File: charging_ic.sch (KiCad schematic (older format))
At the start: 6 parts, among them IC3 MCP73811T-420I_OT, Q1 Q_PMOS_DSG

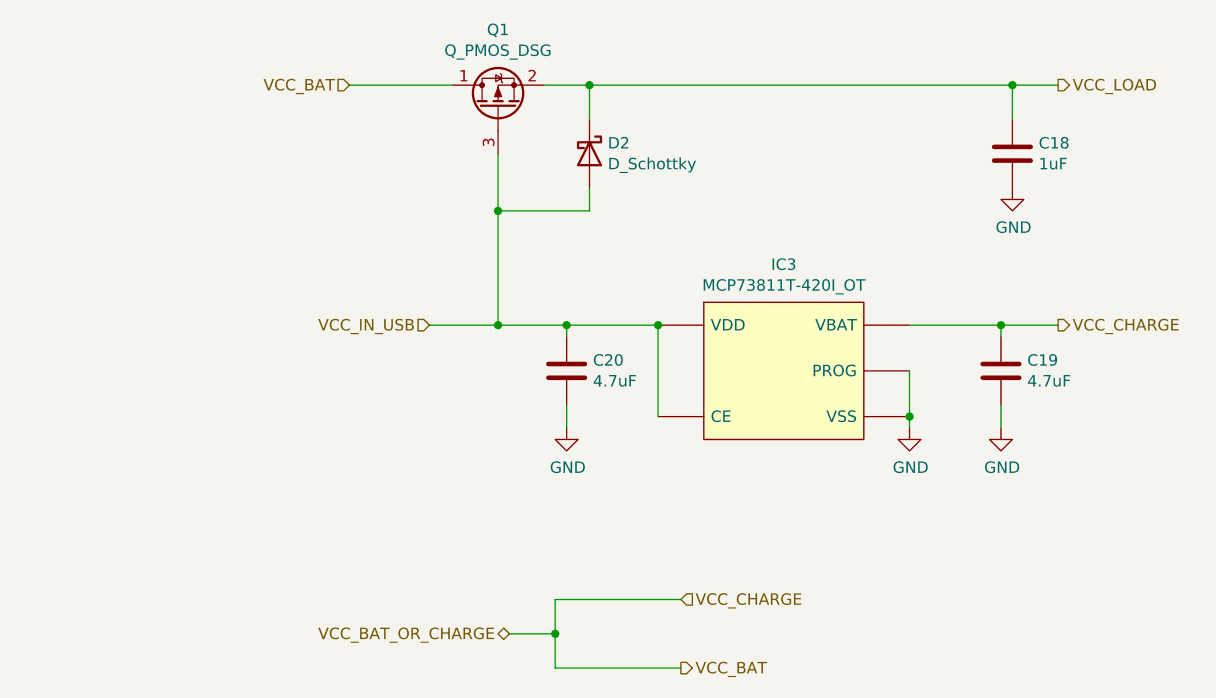
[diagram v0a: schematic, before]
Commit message: Fixed some symbols, assigned some footprints, and made wire labels
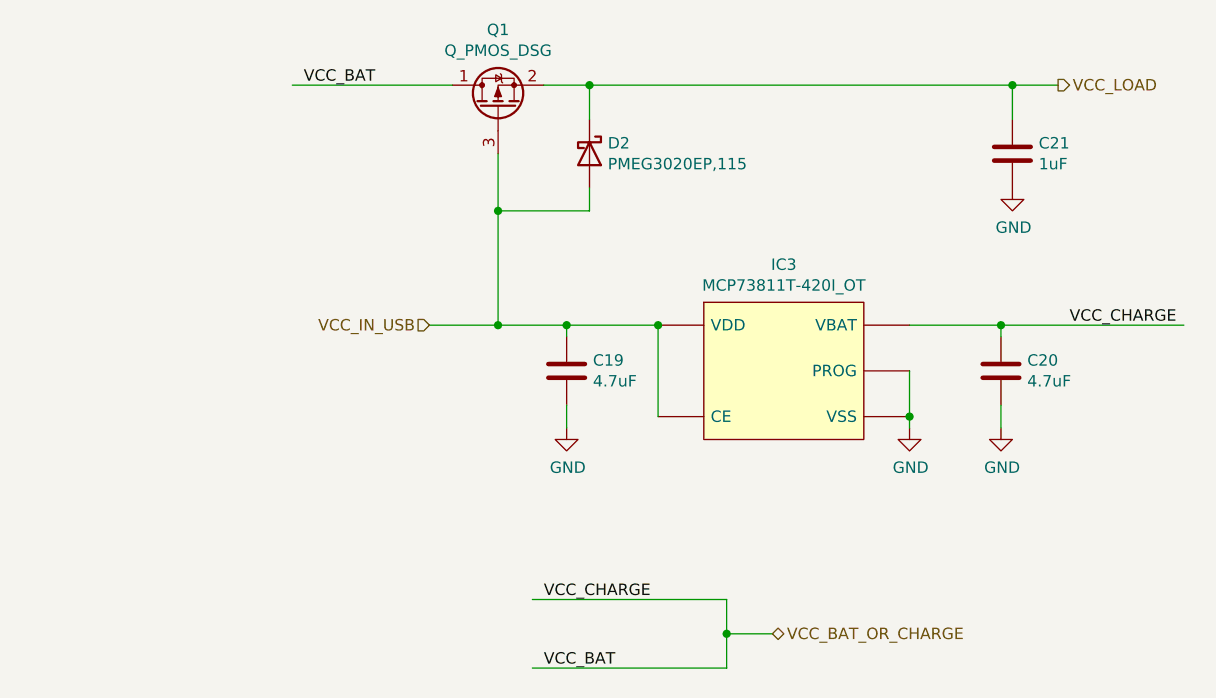
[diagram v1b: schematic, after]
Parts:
- removed D2: D_Schottky, symbol Device:D_Schottky
- added D2: PMEG3020EP,115, Diode_Skywire:SODFL4725X110N, symbol Diode_Shotkey:PMEG3020EP,115
- IC3: footprint SOT95P270X145-5N -> Charging_IC:SOT95P270X145-5N
- renumbered C20 to C19, C19 to C20, C18 to C21
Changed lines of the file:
@@
 F 0 "IC3" H 5650 4115 50  0000 C CNN
 F 1 "MCP73811T-420I_OT" H 5650 4024 50  0000 C CNN
-F 2 "SOT95P270X145-5N" H 5300 3250 50  0001 L CNN
+F 2 "Charging_IC:SOT95P270X145-5N" H 5300 3250 50  0001 L CNN
 F 3 "http://docs-asia.electrocomponents.com/webdocs/0d2b/0900766b80d2b53c.pdf" H 5300 3150 50  0001 L CNN
 F 4 "Li-Ion Charge Controller 4.2V SOT23-5" H 5300 3050 50  0001 L CNN "Description"
@@
 AR Path="/60C41DD6" Ref="#PWR?"  Part="1"
 AR Path="/60BA4931/60C41DD6" Ref="#PWR?"  Part="1"
-AR Path="/60BA4931/60C34886/60C41DD6" Ref="#PWR?"  Part="1"
-F 0 "#PWR?" H 6200 3650 50  0001 C CNN
+AR Path="/60BA4931/60C34886/60C41DD6" Ref="#PWR023"  Part="1"
+F 0 "#PWR023" H 6200 3650 50  0001 C CNN
 F 1 "GND" H 6205 3727 50  0000 C CNN
 F 2 "" H 6200 3900 50  0001 C CNN
@@
 AR Path="/60C41DDC" Ref="#PWR?"  Part="1"
 AR Path="/60BA4931/60C41DDC" Ref="#PWR?"  Part="1"
-AR Path="/60BA4931/60C34886/60C41DDC" Ref="#PWR?"  Part="1"
-F 0 "#PWR?" H 4700 3650 50  0001 C CNN
+AR Path="/60BA4931/60C34886/60C41DDC" Ref="#PWR022"  Part="1"
+F 0 "#PWR022" H 4700 3650 50  0001 C CNN
 F 1 "GND" H 4705 3727 50  0000 C CNN
 F 2 "" H 4700 3900 50  0001 C CNN
@@
 AR Path="/60C41DE3" Ref="C?"  Part="1"
 AR Path="/60BA4931/60C41DE3" Ref="C?"  Part="1"
-AR Path="/60BA4931/60C34886/60C41DE3" Ref="C20"  Part="1"
-F 0 "C20" H 4815 3696 50  0000 L CNN
+AR Path="/60BA4931/60C34886/60C41DE3" Ref="C19"  Part="1"
+F 0 "C19" H 4815 3696 50  0000 L CNN
 F 1 "4.7uF" H 4815 3605 50  0000 L CNN
 F 2 "" H 4738 3500 50  0001 C CNN
@@
 	6600 3450 6600 3500
 Connection ~ 6600 3450
-Wire Wire Line
-	6600 3450 6850 3450
 $Comp
 L power:GND #PWR?
@@
 AR Path="/60C41DEE" Ref="#PWR?"  Part="1"
 AR Path="/60BA4931/60C41DEE" Ref="#PWR?"  Part="1"
-AR Path="/60BA4931/60C34886/60C41DEE" Ref="#PWR?"  Part="1"
-F 0 "#PWR?" H 6600 3650 50  0001 C CNN
+AR Path="/60BA4931/60C34886/60C41DEE" Ref="#PWR024"  Part="1"
+F 0 "#PWR024" H 6600 3650 50  0001 C CNN
 F 1 "GND" H 6605 3727 50  0000 C CNN
 F 2 "" H 6600 3900 50  0001 C CNN
@@
 AR Path="/60C41DF4" Ref="C?"  Part="1"
 AR Path="/60BA4931/60C41DF4" Ref="C?"  Part="1"
-AR Path="/60BA4931/60C34886/60C41DF4" Ref="C19"  Part="1"
-F 0 "C19" H 6715 3696 50  0000 L CNN
+AR Path="/60BA4931/60C34886/60C41DF4" Ref="C20"  Part="1"
+F 0 "C20" H 6715 3696 50  0000 L CNN
 F 1 "4.7uF" H 6715 3605 50  0000 L CNN
 F 2 "" H 6638 3500 50  0001 C CNN
@@
 Wire Wire Line
 	4800 2950 4800 2850
-$Comp
-L Device:D_Schottky D?
-U 1 1 60C41E01
-P 4800 2700
-AR Path="/60C41E01" Ref="D?"  Part="1"
-AR Path="/60BA4931/60C41E01" Ref="D?"  Part="1"
-AR Path="/60BA4931/60C34886/60C41E01" Ref="D2"  Part="1"
-F 0 "D2" V 4754 2780 50  0000 L CNN
-F 1 "D_Schottky" V 4845 2780 50  0000 L CNN
-F 2 "" H 4800 2700 50  0001 C CNN
-F 3 "~" H 4800 2700 50  0001 C CNN
-	1    4800 2700
-	0    1    1    0
-$EndComp
 Wire Wire Line
 	4800 2550 4800 2400
@@
 AR Path="/60C41E10" Ref="#PWR?"  Part="1"
 AR Path="/60BA4931/60C41E10" Ref="#PWR?"  Part="1"
-AR Path="/60BA4931/60C34886/60C41E10" Ref="#PWR?"  Part="1"
-F 0 "#PWR?" H 6650 2600 50  0001 C CNN
+AR Path="/60BA4931/60C34886/60C41E10" Ref="#PWR025"  Part="1"
+F 0 "#PWR025" H 6650 2600 50  0001 C CNN
 F 1 "GND" H 6655 2677 50  0000 C CNN
 F 2 "" H 6650 2850 50  0001 C CNN
@@
 AR Path="/60C41E17" Ref="C?"  Part="1"
 AR Path="/60BA4931/60C41E17" Ref="C?"  Part="1"
-AR Path="/60BA4931/60C34886/60C41E17" Ref="C18"  Part="1"
-F 0 "C18" H 6765 2746 50  0000 L CNN
+AR Path="/60BA4931/60C34886/60C41E17" Ref="C21"  Part="1"
+F 0 "C21" H 6765 2746 50  0000 L CNN
 F 1 "1uF" H 6765 2655 50  0000 L CNN
 F 2 "" H 6688 2550 50  0001 C CNN
@@
 	4400 2700 4400 2950
 Connection ~ 4400 2950
-Wire Wire Line
-	4200 2400 3750 2400
 $Comp
 L Device:Q_PMOS_DSG Q?
@@
 Text HLabel 6850 2400 2    50   Output ~ 0
 VCC_LOAD
-Text HLabel 6850 3450 2    50   Output ~ 0
-VCC_CHARGE
-Text HLabel 3750 2400 0    50   Input ~ 0
-VCC_BAT
 Wire Wire Line
 	4400 3450 4100 3450
@@
 Text HLabel 4100 3450 0    50   Input ~ 0
 VCC_IN_USB
-Wire Wire Line
-	4650 4650 5200 4650
-Wire Wire Line
-	4650 4650 4650 4800
-Wire Wire Line
-	4650 4800 4450 4800
-Connection ~ 4650 4800
-Wire Wire Line
-	4650 4800 4650 4950
-Wire Wire Line
-	4650 4950 5200 4950
-Text HLabel 4450 4800 0    50   BiDi ~ 0
+Text Label 6900 3450 0    50   ~ 0
+VCC_CHARGE
+Wire Wire Line
+	6600 3450 7400 3450
+Wire Wire Line
+	3500 2400 4200 2400
+Text Label 3550 2400 0    50   ~ 0
+VCC_BAT
+Text Label 4600 4950 0    50   ~ 0
+VCC_BAT
+Wire Wire Line
+	4550 4950 5400 4950
+Text Label 4600 4650 0    50   ~ 0
+VCC_CHARGE
+Wire Wire Line
+	4550 4650 5400 4650
+Text HLabel 5600 4800 2    50   BiDi ~ 0
 VCC_BAT_OR_CHARGE
-Text HLabel 5200 4650 2    50   Input ~ 0
-VCC_CHARGE
-Text HLabel 5200 4950 2    50   Output ~ 0
-VCC_BAT
+Wire Wire Line
+	5400 4800 5400 4950
+Connection ~ 5400 4800
+Wire Wire Line
+	5400 4800 5600 4800
+Wire Wire Line
+	5400 4650 5400 4800
+$Comp
+L Diode_Shotkey:PMEG3020EP,115 D2
+U 1 1 6077F670
+P 4800 2700
+F 0 "D2" V 4754 2780 50  0000 L CNN
+F 1 "PMEG3020EP,115" V 4845 2780 50  0000 L CNN
+F 2 "Diode_Skywire:SODFL4725X110N" H 4450 2550 50  0001 L CNN
+F 3 "https://componentsearchengine.com/Datasheets/2/PMEG3020EP,115.pdf" H 4450 2450 50  0001 L CNN
+F 4 "Schottky Diodes & Rectifiers SCHOTTKY RECT 30V 2A" H 4450 2350 50  0001 L CNN "Description"
+F 5 "1.1" H 4450 2250 50  0001 L CNN "Height"
+F 6 "Nexperia" H 4450 2150 50  0001 L CNN "Manufacturer_Name"
+F 7 "PMEG3020EP,115" H 4450 2050 50  0001 L CNN "Manufacturer_Part_Number"
+F 8 "771-PMEG3020EP115" H 4450 1950 50  0001 L CNN "Mouser Part Number"
+F 9 "https://www.mouser.co.uk/ProductDetail/Nexperia/PMEG3020EP115/?qs=GcY6OjH1zdnlY%252B06tUqEyw%3D%3D" H 4450 1850 50  0001 L CNN "Mouser Price/Stock"
+F 10 "PMEG3020EP,115" H 4450 1750 50  0001 L CNN "Arrow Part Number"
+F 11 "https://www.arrow.com/en/products/pmeg3020ep115/nexperia" H 4450 1650 50  0001 L CNN "Arrow Price/Stock"
+	1    4800 2700
+	0    1    1    0
+$EndComp
 $EndSCHEMATC

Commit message: Finished annotations and assigned more footprints, electrical rules check is marked good
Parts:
- added R15: 10k, symbol Device:R_US
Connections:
- wire segments 27 -> 29
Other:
- moved on the sheet: C19, Q1
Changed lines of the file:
@@
 $EndComp
 Wire Wire Line
-	5100 3450 4700 3450
+	5100 3450 4650 3450
 Wire Wire Line
 	5100 3850 5100 3450
@@
 L power:GND #PWR?
 U 1 1 60C41DDC
-P 4700 3900
+P 4650 3900
 AR Path="/60C41DDC" Ref="#PWR?"  Part="1"
 AR Path="/60BA4931/60C41DDC" Ref="#PWR?"  Part="1"
 AR Path="/60BA4931/60C34886/60C41DDC" Ref="#PWR022"  Part="1"
-F 0 "#PWR022" H 4700 3650 50  0001 C CNN
-F 1 "GND" H 4705 3727 50  0000 C CNN
-F 2 "" H 4700 3900 50  0001 C CNN
-F 3 "" H 4700 3900 50  0001 C CNN
-	1    4700 3900
-	1    0    0    -1
-$EndComp
-Wire Wire Line
-	4700 3450 4700 3500
+F 0 "#PWR022" H 4650 3650 50  0001 C CNN
+F 1 "GND" H 4655 3727 50  0000 C CNN
+F 2 "" H 4650 3900 50  0001 C CNN
+F 3 "" H 4650 3900 50  0001 C CNN
+	1    4650 3900
+	1    0    0    -1
+$EndComp
+Wire Wire Line
+	4650 3450 4650 3550
 $Comp
 L Device:C C?
 U 1 1 60C41DE3
-P 4700 3650
+P 4650 3700
 AR Path="/60C41DE3" Ref="C?"  Part="1"
 AR Path="/60BA4931/60C41DE3" Ref="C?"  Part="1"
 AR Path="/60BA4931/60C34886/60C41DE3" Ref="C19"  Part="1"
-F 0 "C19" H 4815 3696 50  0000 L CNN
-F 1 "4.7uF" H 4815 3605 50  0000 L CNN
-F 2 "" H 4738 3500 50  0001 C CNN
-F 3 "~" H 4700 3650 50  0001 C CNN
-	1    4700 3650
-	1    0    0    -1
-$EndComp
-Wire Wire Line
-	4700 3800 4700 3900
+F 0 "C19" H 4765 3746 50  0000 L CNN
+F 1 "4.7uF" H 4765 3655 50  0000 L CNN
+F 2 "" H 4688 3550 50  0001 C CNN
+F 3 "~" H 4650 3700 50  0001 C CNN
+	1    4650 3700
+	1    0    0    -1
+$EndComp
+Wire Wire Line
+	4650 3850 4650 3900
 Wire Wire Line
 	6200 3450 6600 3450
@@
 Wire Wire Line
 	6600 3800 6600 3900
-Connection ~ 4700 3450
-Wire Wire Line
-	4400 2950 4800 2950
+Connection ~ 4650 3450
+Wire Wire Line
+	4150 2950 4800 2950
 Wire Wire Line
 	4800 2950 4800 2850
@@
 	6650 2400 6850 2400
 Wire Wire Line
-	4400 3450 4700 3450
+	4150 3450 4650 3450
 $Comp
 L power:GND #PWR?
@@
 $EndComp
 Wire Wire Line
-	4400 2950 4400 3450
-Wire Wire Line
-	4600 2400 4800 2400
+	4150 2950 4150 3450
+Wire Wire Line
+	4350 2400 4800 2400
 Connection ~ 4800 2400
 Wire Wire Line
-	4400 2700 4400 2950
-Connection ~ 4400 2950
+	4150 2700 4150 2950
+Connection ~ 4150 2950
 $Comp
 L Device:Q_PMOS_DSG Q?
 U 1 1 60C41E23
-P 4400 2500
+P 4150 2500
 AR Path="/60C41E23" Ref="Q?"  Part="1"
 AR Path="/60BA4931/60C41E23" Ref="Q?"  Part="1"
 AR Path="/60BA4931/60C34886/60C41E23" Ref="Q1"  Part="1"
-F 0 "Q1" V 4742 2500 50  0000 C CNN
-F 1 "Q_PMOS_DSG" V 4651 2500 50  0000 C CNN
-F 2 "" H 4600 2600 50  0001 C CNN
-F 3 "~" H 4400 2500 50  0001 C CNN
-	1    4400 2500
+F 0 "Q1" V 4492 2500 50  0000 C CNN
+F 1 "Q_PMOS_DSG" V 4401 2500 50  0000 C CNN
+F 2 "" H 4350 2600 50  0001 C CNN
+F 3 "~" H 4150 2500 50  0001 C CNN
+	1    4150 2500
 	0    -1   -1   0
 $EndComp
@@
 VCC_LOAD
 Wire Wire Line
-	4400 3450 4100 3450
-Connection ~ 4400 3450
-Text HLabel 4100 3450 0    50   Input ~ 0
+	4150 3450 3850 3450
+Connection ~ 4150 3450
+Text HLabel 3850 3450 0    50   Input ~ 0
 VCC_IN_USB
 Text Label 6900 3450 0    50   ~ 0
@@
 	6600 3450 7400 3450
 Wire Wire Line
-	3500 2400 4200 2400
-Text Label 3550 2400 0    50   ~ 0
+	3250 2400 3950 2400
+Text Label 3300 2400 0    50   ~ 0
 VCC_BAT
 Text Label 4600 4950 0    50   ~ 0
@@
 	0    1    1    0
 $EndComp
+Wire Wire Line
+	4150 3450 4150 3550
+$Comp
+L power:GND #PWR030
+U 1 1 606A84E4
+P 4150 3900
+F 0 "#PWR030" H 4150 3650 50  0001 C CNN
+F 1 "GND" H 4155 3727 50  0000 C CNN
+F 2 "" H 4150 3900 50  0001 C CNN
+F 3 "" H 4150 3900 50  0001 C CNN
+	1    4150 3900
+	1    0    0    -1
+$EndComp
+$Comp
+L Device:R_US R15
+U 1 1 606A9537
+P 4150 3700
+F 0 "R15" H 4218 3746 50  0000 L CNN
+F 1 "10k" H 4218 3655 50  0000 L CNN
+F 2 "" V 4190 3690 50  0001 C CNN
+F 3 "~" H 4150 3700 50  0001 C CNN
+	1    4150 3700
+	1    0    0    -1
+$EndComp
+Wire Wire Line
+	4150 3850 4150 3900
 $EndSCHEMATC

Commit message: Chose more parts and added more footprints. Have some resistors and all the capacitors to go
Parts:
- removed Q1: Q_PMOS_DSG, symbol Device:Q_PMOS_DSG
- added Q1: CSD25402Q3AT, Mosfet_TI:CSD25402Q3AT, symbol PMosfet:CSD25402Q3AT
- R15: footprint (none) -> Resistor_SMD:R_0402_1005Metric
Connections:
- wire segments 29 -> 44
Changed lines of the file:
@@
 Wire Wire Line
 	4150 2950 4150 3450
-Wire Wire Line
-	4350 2400 4800 2400
-Connection ~ 4800 2400
-Wire Wire Line
-	4150 2700 4150 2950
-Connection ~ 4150 2950
-$Comp
-L Device:Q_PMOS_DSG Q?
-U 1 1 60C41E23
-P 4150 2500
-AR Path="/60C41E23" Ref="Q?"  Part="1"
-AR Path="/60BA4931/60C41E23" Ref="Q?"  Part="1"
-AR Path="/60BA4931/60C34886/60C41E23" Ref="Q1"  Part="1"
-F 0 "Q1" V 4492 2500 50  0000 C CNN
-F 1 "Q_PMOS_DSG" V 4401 2500 50  0000 C CNN
-F 2 "" H 4350 2600 50  0001 C CNN
-F 3 "~" H 4150 2500 50  0001 C CNN
-	1    4150 2500
-	0    -1   -1   0
-$EndComp
 Text HLabel 6850 2400 2    50   Output ~ 0
 VCC_LOAD
 Wire Wire Line
-	4150 3450 3850 3450
+	4150 3450 3550 3450
 Connection ~ 4150 3450
-Text HLabel 3850 3450 0    50   Input ~ 0
+Text HLabel 3550 3450 0    50   Input ~ 0
 VCC_IN_USB
 Text Label 6900 3450 0    50   ~ 0
@@
 Wire Wire Line
 	6600 3450 7400 3450
-Wire Wire Line
-	3250 2400 3950 2400
-Text Label 3300 2400 0    50   ~ 0
+Text Label 2350 2400 0    50   ~ 0
 VCC_BAT
 Text Label 4600 4950 0    50   ~ 0
@@
 F 0 "R15" H 4218 3746 50  0000 L CNN
 F 1 "10k" H 4218 3655 50  0000 L CNN
-F 2 "" V 4190 3690 50  0001 C CNN
+F 2 "Resistor_SMD:R_0402_1005Metric" V 4190 3690 50  0001 C CNN
 F 3 "~" H 4150 3700 50  0001 C CNN
 	1    4150 3700
@@
 Wire Wire Line
 	4150 3850 4150 3900
+$Comp
+L PMosfet:CSD25402Q3AT Q1
+U 1 1 60723D24
+P 3550 2600
+F 0 "Q1" H 3550 3065 50  0000 C CNN
+F 1 "CSD25402Q3AT" H 3550 2974 50  0000 C CNN
+F 2 "Mosfet_TI:CSD25402Q3AT" H 3250 2150 50  0001 L CNN
+F 3 "https://www.ti.com/lit/gpn/CSD25402Q3A" H 3250 2050 50  0001 L CNN
+F 4 "MOSFET -20V, P ch NexFET MOSFET , single SON 3x3, 8.9mOhm 8-VSONP -55 to 150" H 3250 1950 50  0001 L CNN "Description"
+F 5 "0.9" H 3250 1850 50  0001 L CNN "Height"
+F 6 "Texas Instruments" H 3250 1750 50  0001 L CNN "Manufacturer_Name"
+F 7 "CSD25402Q3AT" H 3250 1650 50  0001 L CNN "Manufacturer_Part_Number"
+F 8 "595-CSD25402Q3AT" H 3250 1550 50  0001 L CNN "Mouser Part Number"
+F 9 "https://www.mouser.co.uk/ProductDetail/Texas-Instruments/CSD25402Q3AT/?qs=Cb2nCFKsA8rIEmINOYCi9A%3D%3D" H 3250 1450 50  0001 L CNN "Mouser Price/Stock"
+F 10 "CSD25402Q3AT" H 3250 1350 50  0001 L CNN "Arrow Part Number"
+F 11 "https://www.arrow.com/en/products/csd25402q3at/texas-instruments" H 3250 1250 50  0001 L CNN "Arrow Price/Stock"
+	1    3550 2600
+	-1   0    0    1
+$EndComp
+Wire Wire Line
+	4050 2600 4150 2600
+Wire Wire Line
+	4150 2600 4150 2500
+Wire Wire Line
+	4150 2400 4050 2400
+Wire Wire Line
+	4050 2500 4150 2500
+Connection ~ 4150 2500
+Wire Wire Line
+	4150 2500 4150 2400
+Wire Wire Line
+	3050 2400 2950 2400
+Wire Wire Line
+	2950 2800 3050 2800
+Wire Wire Line
+	3050 2700 2950 2700
+Connection ~ 2950 2700
+Wire Wire Line
+	2950 2700 2950 2800
+Wire Wire Line
+	3050 2600 2950 2600
+Connection ~ 2950 2600
+Wire Wire Line
+	2950 2600 2950 2700
+Wire Wire Line
+	2950 2400 2950 2500
+Wire Wire Line
+	3050 2500 2950 2500
+Connection ~ 2950 2500
+Wire Wire Line
+	2950 2500 2950 2600
+Connection ~ 2950 2400
+Wire Wire Line
+	2300 2400 2950 2400
+Wire Wire Line
+	4150 2400 4800 2400
+Connection ~ 4150 2400
+Connection ~ 4800 2400
+Wire Wire Line
+	4150 2950 4150 2800
+Wire Wire Line
+	4150 2800 4050 2800
+Connection ~ 4150 2950
 $EndSCHEMATC

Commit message: Finished assigning footprints, and generated netlist
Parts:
- C19, C20, C21: footprint (none) -> Capacitor_SMD:C_0603_1608Metric
- R15: footprint Resistor_SMD:R_0402_1005Metric -> Resistor_SMD:R_1206_3216Metric
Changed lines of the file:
@@
 F 0 "C19" H 4765 3746 50  0000 L CNN
 F 1 "4.7uF" H 4765 3655 50  0000 L CNN
-F 2 "" H 4688 3550 50  0001 C CNN
+F 2 "Capacitor_SMD:C_0603_1608Metric" H 4688 3550 50  0001 C CNN
 F 3 "~" H 4650 3700 50  0001 C CNN
 	1    4650 3700
@@
 F 0 "C20" H 6715 3696 50  0000 L CNN
 F 1 "4.7uF" H 6715 3605 50  0000 L CNN
-F 2 "" H 6638 3500 50  0001 C CNN
+F 2 "Capacitor_SMD:C_0603_1608Metric" H 6638 3500 50  0001 C CNN
 F 3 "~" H 6600 3650 50  0001 C CNN
 	1    6600 3650
@@
 F 0 "C21" H 6765 2746 50  0000 L CNN
 F 1 "1uF" H 6765 2655 50  0000 L CNN
-F 2 "" H 6688 2550 50  0001 C CNN
+F 2 "Capacitor_SMD:C_0603_1608Metric" H 6688 2550 50  0001 C CNN
 F 3 "~" H 6650 2700 50  0001 C CNN
 	1    6650 2700
@@
 F 0 "R15" H 4218 3746 50  0000 L CNN
 F 1 "10k" H 4218 3655 50  0000 L CNN
-F 2 "Resistor_SMD:R_0402_1005Metric" V 4190 3690 50  0001 C CNN
+F 2 "Resistor_SMD:R_1206_3216Metric" V 4190 3690 50  0001 C CNN
 F 3 "~" H 4150 3700 50  0001 C CNN
 	1    4150 3700
